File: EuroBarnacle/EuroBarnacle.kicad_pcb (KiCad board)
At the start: 2 copper layers, 138.4 x 110.1 mm, 60 parts

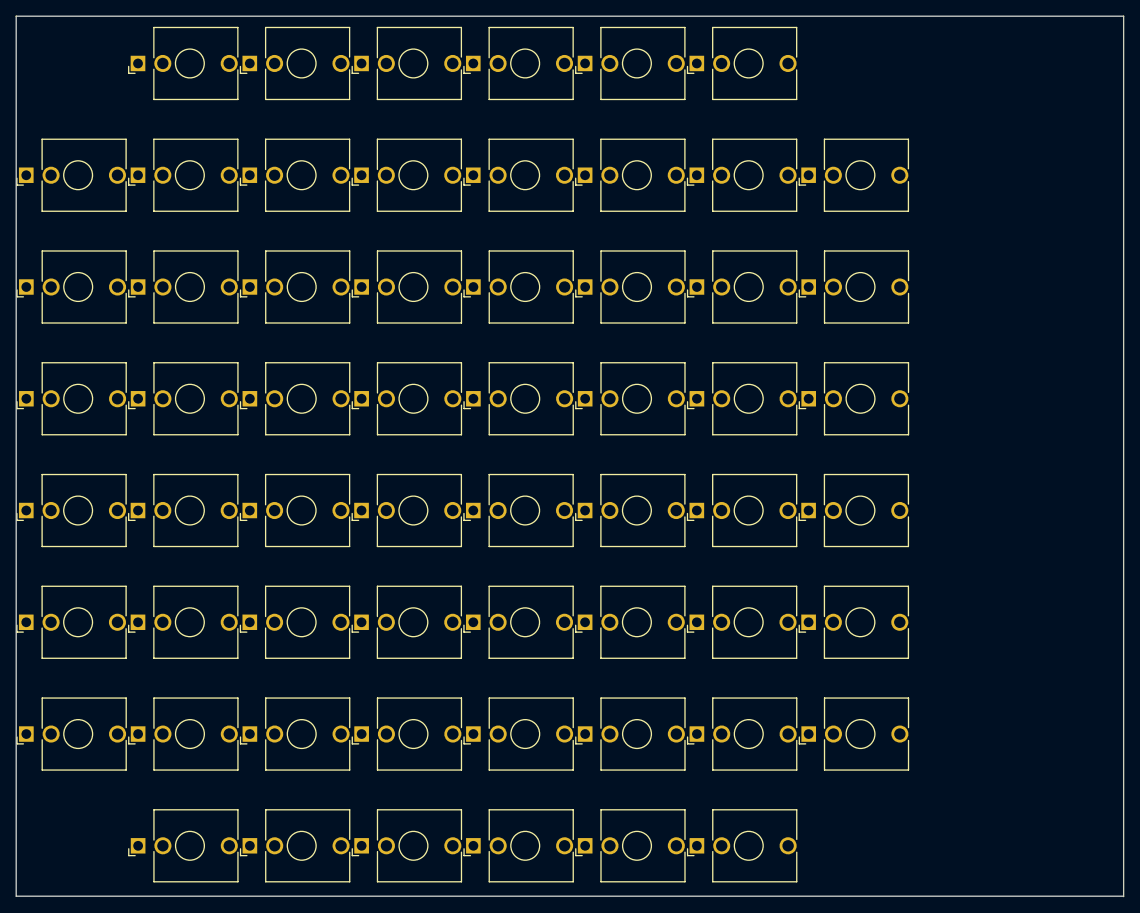
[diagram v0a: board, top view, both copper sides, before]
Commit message: Add Edge Connector
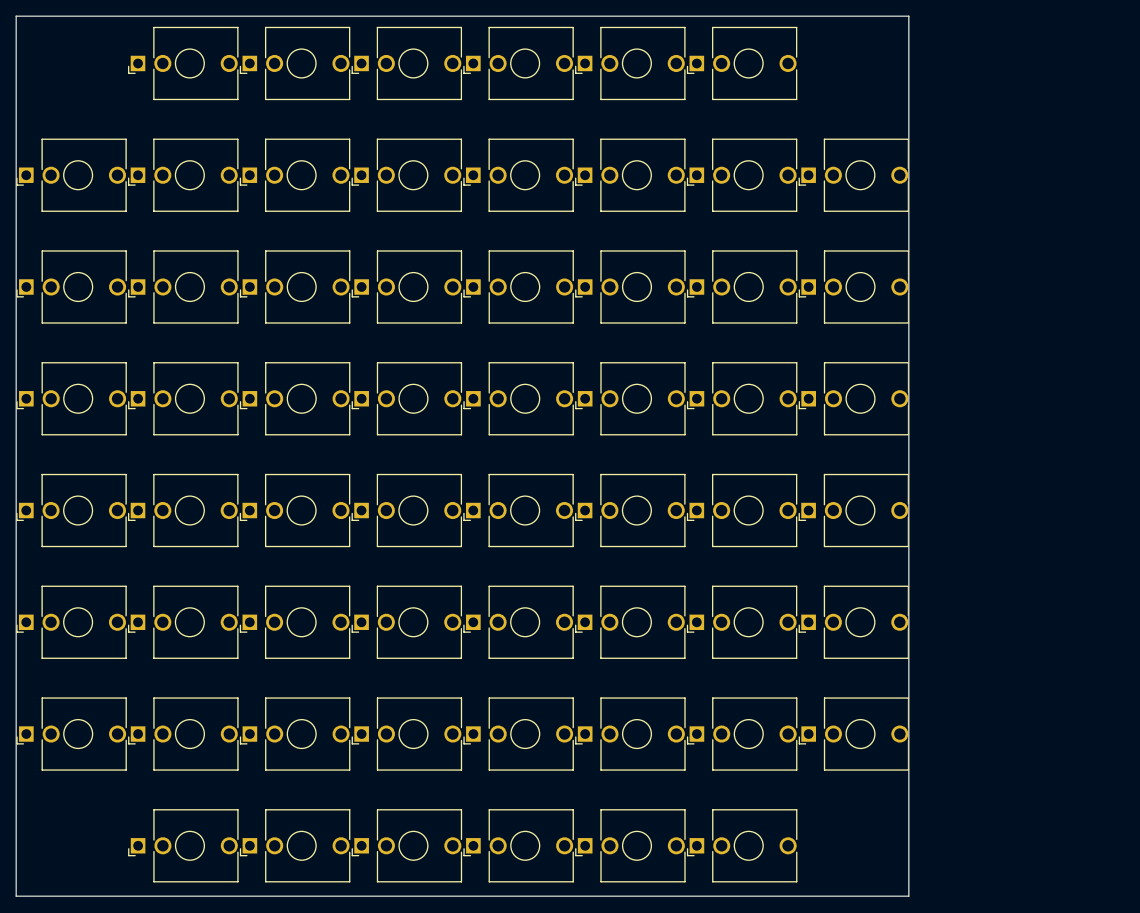
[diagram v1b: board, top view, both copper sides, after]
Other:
- board size 138.4 x 110.1 mm -> 111.6 x 110 mm
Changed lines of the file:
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@@
 	(gr_line
 		(start 58.42 146)
-		(end 196.85 146)
+		(end 170 146)
 		(stroke
 			(width 0.05)
@@
 	)
 	(gr_line
-		(start 196.85 146.05)
-		(end 196.85 36)
+		(start 170 146)
+		(end 170 36)
 		(stroke
 			(width 0.05)
@@
 	)
 	(gr_line
-		(start 196.85 36)
+		(start 170 36)
 		(end 58.42 36)
 		(stroke
